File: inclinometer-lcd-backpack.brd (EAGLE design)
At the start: 78.7 x 25.4 mm, 15 parts, among them IC1 ATmega328-DIP-Prgrammed, Q1 2N3904, U1 LCD-16X2NOHOLES, Y1 16MHz

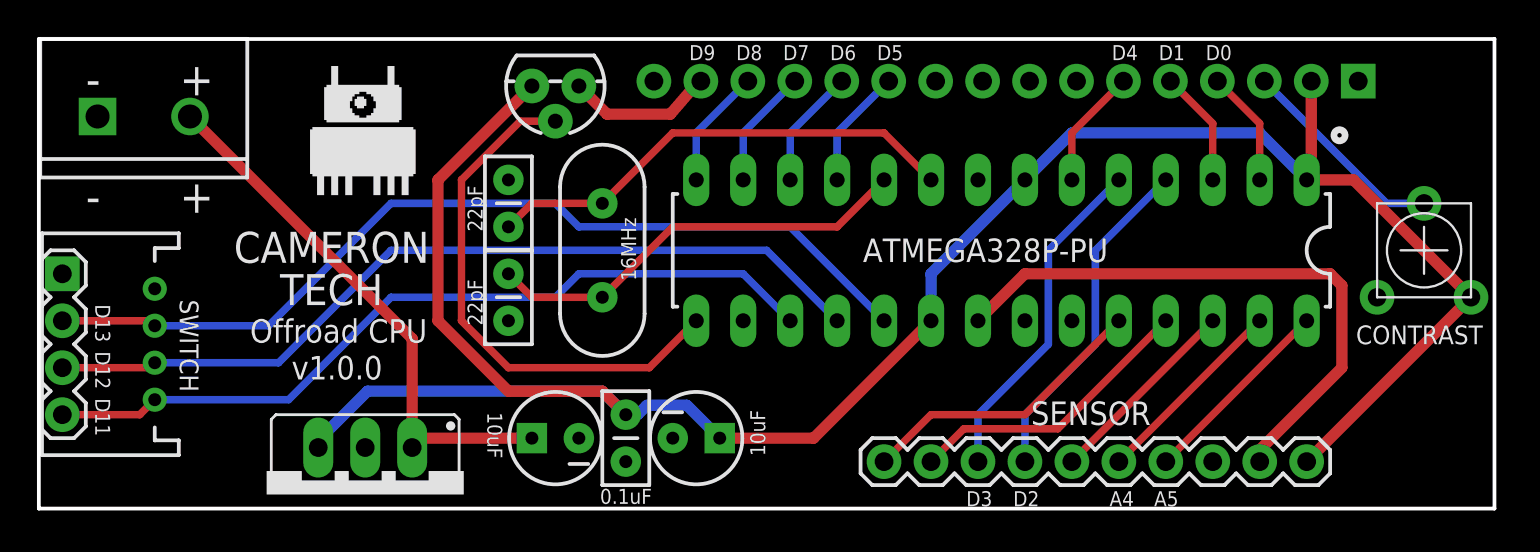
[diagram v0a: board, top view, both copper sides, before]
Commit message: Moves ATMEGA a tad so it's easier to remove, updates silkscreens on some pins
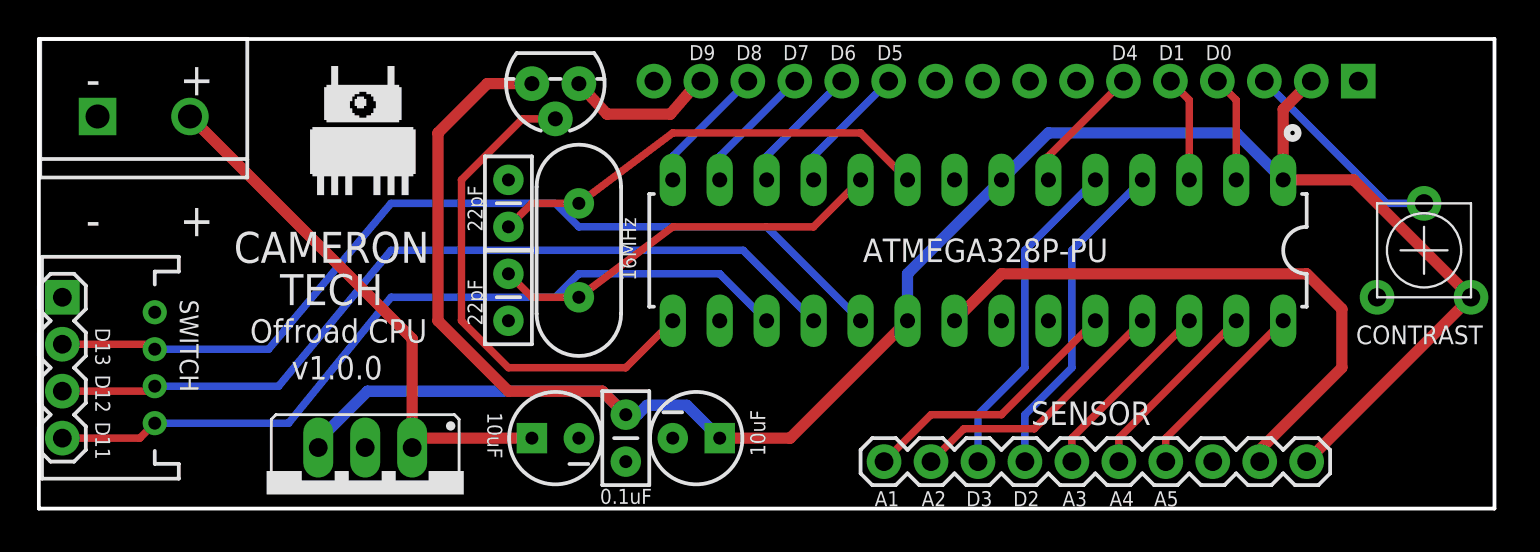
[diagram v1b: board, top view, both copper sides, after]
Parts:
- Q1: device SparkFun:TO-92 -> SparkFun-DiscreteSemi:TO-92
- moved IC1 1.27 mm to (50.8, 14.0)
- moved SWITCH-JST 1.27 mm to (1.27, 7.62)
- moved SWITCH 1.27 mm to (1.27, 11.4)
- moved Y1 1.27 mm to (29.2, 14.0)
- moved Q1 0.13 mm to (27.9, 23.0)
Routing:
- net 5V: track 122.4 -> 124.5 mm
- net XTAL2: track 23.5 -> 21.9 mm
- net XTAL1: track 26.0 -> 24.4 mm
- net A2: track 15.9 -> 14.6 mm
- net A1: track 15.9 -> 14.6 mm
- net BL-EN: track 28.8 -> 27.6 mm
- net A4: track 10.8 -> 10.3 mm
- net RS: track 6.29 -> 5.76 mm
- net INT0: track 18.4 -> 17.9 mm
- net A3: track 10.8 -> 10.3 mm
- net E: track 6.50 -> 7.02 mm
- net DB7: track 6.50 -> 7.02 mm
- net DB6: track 6.50 -> 7.02 mm
- net DB5: track 6.50 -> 7.02 mm
- net DB4: track 6.50 -> 7.02 mm
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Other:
- board text added: "A1"
- board text added: "A2"
- board text added: "A3"
- board text added: "http://git.io/offroadcpu"
- board text removed: "CTORD100"
- board text removed: "http://git.io/incline"
